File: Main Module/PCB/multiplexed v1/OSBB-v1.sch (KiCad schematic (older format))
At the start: 21 parts, among them P1 AUX 1-3, P14 EXTRA Pins, P2 Wire to Teensy VUSB, P3 +3.3V, P4 Pit limiter, P5 Rotary Encoders, P6 BTN 1-32, Q1 Q_NPN_CBE, Q2 Q_NPN_CBE, Q3 Q_NPN_CBE, U1 74HC4051, U2 74HC4051, U3 74HC4051, U4 74HC4051, U5 Teensy3.2

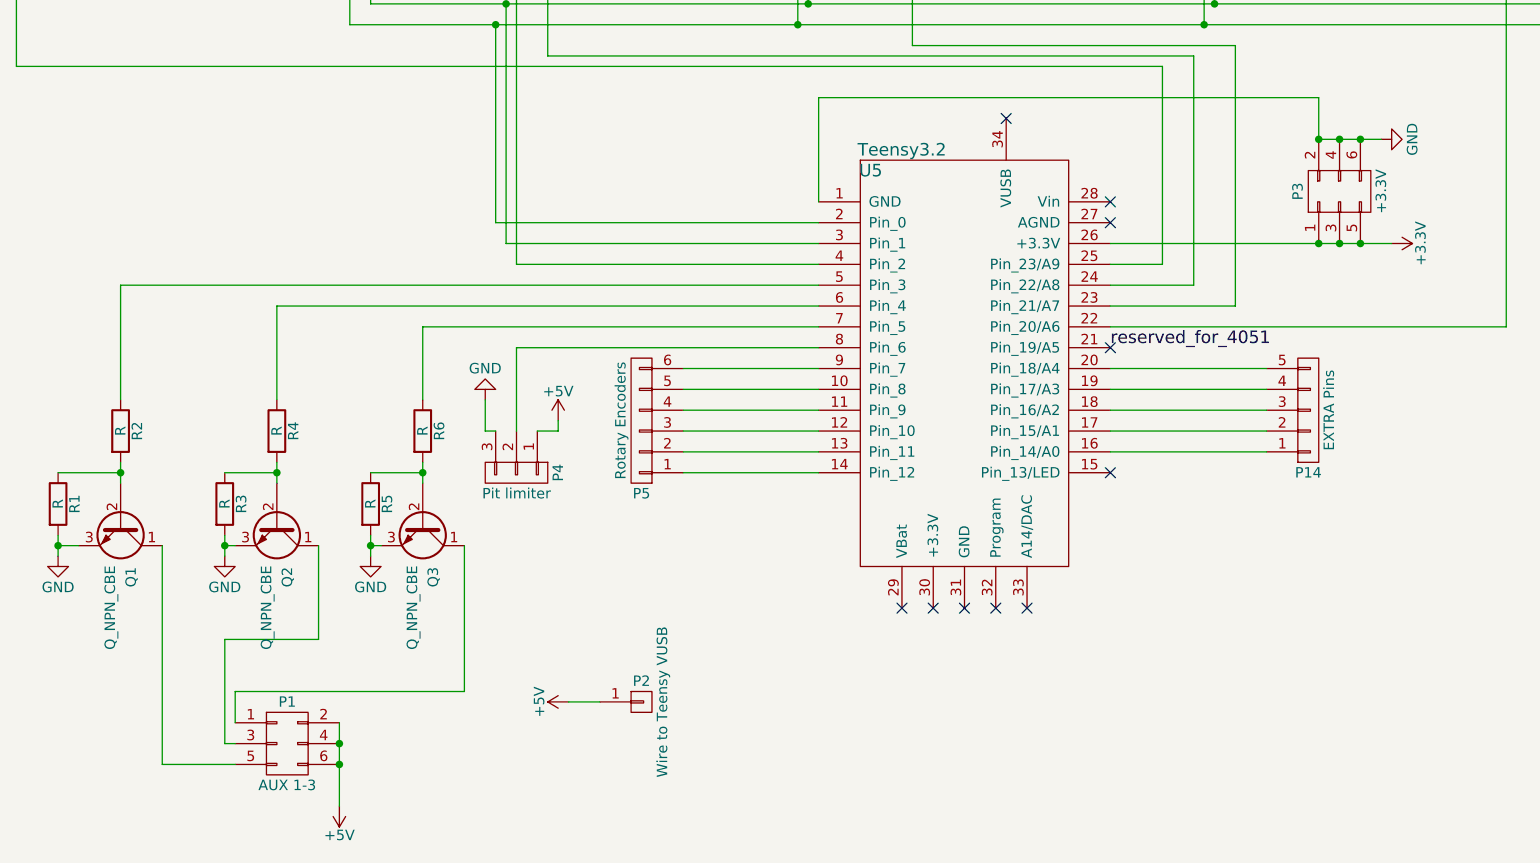
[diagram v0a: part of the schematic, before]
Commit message: * added circuit for pit limiter switch onto the PCB * added open HW logo
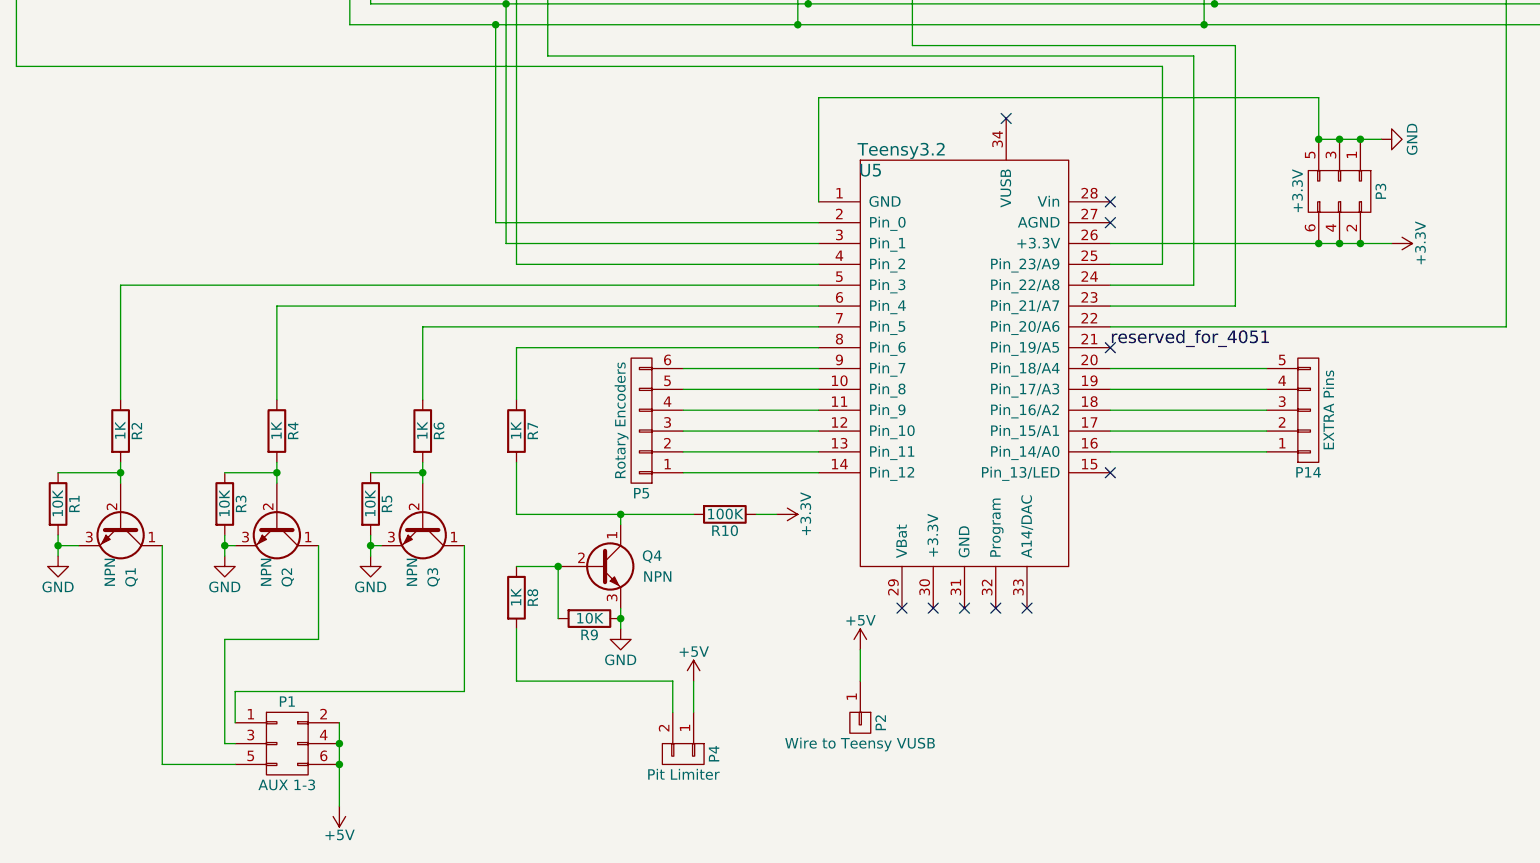
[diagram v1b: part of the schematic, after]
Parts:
- removed P4: Pit limiter, Pin_Headers:Pin_Header_Angled_1x03, symbol CONN_01X03
- added P4: Pit Limiter, Pin_Headers:Pin_Header_Angled_1x02, symbol CONN_01X02
- added Q4: NPN, TO_SOT_Packages_THT:TO-92_Inline_Narrow_Oval, symbol Q_NPN_CBE
- added R10: 100K, Resistors_ThroughHole:Resistor_Horizontal_RM7mm, symbol R
- added R7, R8: 1K, Resistors_ThroughHole:Resistor_Horizontal_RM7mm, symbol R
- added R9: 10K, Resistors_ThroughHole:Resistor_Horizontal_RM7mm, symbol R
- Q1, Q2, Q3: value Q_NPN_CBE -> NPN
- R1, R3, R5: value R -> 10K
- R2, R4, R6: value R -> 1K
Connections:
- net +3V3: now also P3.2 (P2), P3.4 (P4), P3.6 (P6), R10.1; no longer P3.1 (P1), P3.3 (P3), P3.5 (P5)
- net +5V: now also P4.1 (P1)
- net GND: now also P3.1 (P1), P3.3 (P3), P3.5 (P5), Q4.3 (E), R9.1; no longer P3.2 (P2), P3.4 (P4), P3.6 (P6)
- net at U5.8 (Pin_6): now also R7.1
- new net: Q4.1 (C), R10.2, R7.2
- new net: Q4.2 (B), R8.1, R9.2
- new net: P4.2 (P2), R8.2
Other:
- moved on the sheet: P2
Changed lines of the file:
@@
 P 1200 6000
 F 0 "Q1" H 1500 6050 50  0000 R CNN
-F 1 "Q_NPN_CBE" H 1800 5950 50  0000 R CNN
+F 1 "NPN" H 1500 5950 50  0000 R CNN
 F 2 "TO_SOT_Packages_THT:TO-92_Inline_Narrow_Oval" H 1400 6100 50  0001 C CNN
 F 3 "" H 1200 6000 50  0000 C CNN
@@
 P 1950 6000
 F 0 "Q2" H 2250 6050 50  0000 R CNN
-F 1 "Q_NPN_CBE" H 2550 5950 50  0000 R CNN
+F 1 "NPN" H 2250 5950 50  0000 R CNN
 F 2 "TO_SOT_Packages_THT:TO-92_Inline_Narrow_Oval" H 2150 6100 50  0001 C CNN
 F 3 "" H 1950 6000 50  0000 C CNN
@@
 P 2650 6000
 F 0 "Q3" H 2950 6050 50  0000 R CNN
-F 1 "Q_NPN_CBE" H 3250 5950 50  0000 R CNN
+F 1 "NPN" H 2950 5950 50  0000 R CNN
 F 2 "TO_SOT_Packages_THT:TO-92_Inline_Narrow_Oval" H 2850 6100 50  0001 C CNN
 F 3 "" H 2650 6000 50  0000 C CNN
@@
 P 1200 5550
 F 0 "R2" V 1280 5550 50  0000 C CNN
-F 1 "R" V 1200 5550 50  0000 C CNN
+F 1 "1K" V 1200 5550 50  0000 C CNN
 F 2 "Resistors_ThroughHole:Resistor_Horizontal_RM7mm" V 1130 5550 50  0001 C CNN
 F 3 "" H 1200 5550 50  0000 C CNN
@@
 P 1950 5550
 F 0 "R4" V 2030 5550 50  0000 C CNN
-F 1 "R" V 1950 5550 50  0000 C CNN
+F 1 "1K" V 1950 5550 50  0000 C CNN
 F 2 "Resistors_ThroughHole:Resistor_Horizontal_RM7mm" V 1880 5550 50  0001 C CNN
 F 3 "" H 1950 5550 50  0000 C CNN
@@
 P 2650 5550
 F 0 "R6" V 2730 5550 50  0000 C CNN
-F 1 "R" V 2650 5550 50  0000 C CNN
+F 1 "1K" V 2650 5550 50  0000 C CNN
 F 2 "Resistors_ThroughHole:Resistor_Horizontal_RM7mm" V 2580 5550 50  0001 C CNN
 F 3 "" H 2650 5550 50  0000 C CNN
@@
 P 900 5900
 F 0 "R1" V 980 5900 50  0000 C CNN
-F 1 "R" V 900 5900 50  0000 C CNN
+F 1 "10K" V 900 5900 50  0000 C CNN
 F 2 "Resistors_ThroughHole:Resistor_Horizontal_RM7mm" V 830 5900 50  0001 C CNN
 F 3 "" H 900 5900 50  0000 C CNN
@@
 P 1700 5900
 F 0 "R3" V 1780 5900 50  0000 C CNN
-F 1 "R" V 1700 5900 50  0000 C CNN
+F 1 "10K" V 1700 5900 50  0000 C CNN
 F 2 "Resistors_ThroughHole:Resistor_Horizontal_RM7mm" V 1630 5900 50  0001 C CNN
 F 3 "" H 1700 5900 50  0000 C CNN
@@
 P 2400 5900
 F 0 "R5" V 2480 5900 50  0000 C CNN
-F 1 "R" V 2400 5900 50  0000 C CNN
+F 1 "10K" V 2400 5900 50  0000 C CNN
 F 2 "Resistors_ThroughHole:Resistor_Horizontal_RM7mm" V 2330 5900 50  0001 C CNN
 F 3 "" H 2400 5900 50  0000 C CNN
@@
 $EndComp
 $Comp
-L CONN_01X03 P4
-U 1 1 581036AC
-P 3100 5750
-F 0 "P4" H 3100 5950 50  0000 C CNN
-F 1 "Pit limiter" V 3200 5750 50  0000 C CNN
-F 2 "Pin_Headers:Pin_Header_Angled_1x03" H 3100 5750 50  0001 C CNN
-F 3 "" H 3100 5750 50  0000 C CNN
-	1    3100 5750
-	0    1    1    0
-$EndComp
-$Comp
 L GND #PWR04
 U 1 1 5810375B
-P 2950 5400
-F 0 "#PWR04" H 2950 5150 50  0001 C CNN
-F 1 "GND" H 2950 5250 50  0000 C CNN
-F 2 "" H 2950 5400 50  0000 C CNN
-F 3 "" H 2950 5400 50  0000 C CNN
-	1    2950 5400
-	-1   0    0    1
+P 3600 6500
+F 0 "#PWR04" H 3600 6250 50  0001 C CNN
+F 1 "GND" H 3600 6350 50  0000 C CNN
+F 2 "" H 3600 6500 50  0000 C CNN
+F 3 "" H 3600 6500 50  0000 C CNN
+	1    3600 6500
+	1    0    0    -1
 $EndComp
 $Comp
 L +5V #PWR05
 U 1 1 581037AF
-P 3300 5500
-F 0 "#PWR05" H 3300 5350 50  0001 C CNN
-F 1 "+5V" H 3300 5640 50  0000 C CNN
-F 2 "" H 3300 5500 50  0000 C CNN
-F 3 "" H 3300 5500 50  0000 C CNN
-	1    3300 5500
+P 3950 6750
+F 0 "#PWR05" H 3950 6600 50  0001 C CNN
+F 1 "+5V" H 3950 6890 50  0000 C CNN
+F 2 "" H 3950 6750 50  0000 C CNN
+F 3 "" H 3950 6750 50  0000 C CNN
+	1    3950 6750
 	1    0    0    -1
 $EndComp
@@
 	3100 5150 4550 5150
 Wire Wire Line
-	3100 5150 3100 5550
+	3100 5150 3100 5400
 Wire Wire Line
 	6350 3750 6350 4850
 Wire Wire Line
 	700  3800 6200 3800
-Wire Wire Line
-	3000 5550 2950 5550
-Wire Wire Line
-	2950 5550 2950 5400
-Wire Wire Line
-	3200 5550 3300 5550
-Wire Wire Line
-	3300 5550 3300 5500
 Wire Wire Line
 	6200 4750 5950 4750
@@
 L CONN_01X01 P2
 U 1 1 58126797
-P 3700 6850
-F 0 "P2" H 3700 6950 50  0000 C CNN
-F 1 "Wire to Teensy VUSB" V 3800 6850 50  0000 C CNN
-F 2 "Pin_Headers:Pin_Header_Straight_1x01" H 3700 6850 50  0001 C CNN
-F 3 "" H 3700 6850 50  0000 C CNN
-	1    3700 6850
-	1    0    0    -1
+P 4750 6950
+F 0 "P2" H 4750 7050 50  0000 C CNN
+F 1 "Wire to Teensy VUSB" V 4850 6950 50  0000 C CNN
+F 2 "Pin_Headers:Pin_Header_Straight_1x01" H 4750 6950 50  0001 C CNN
+F 3 "" H 4750 6950 50  0000 C CNN
+	1    4750 6950
+	0    1    1    0
 $EndComp
 $Comp
 L +5V #PWR07
 U 1 1 581272E3
-P 3350 6850
-F 0 "#PWR07" H 3350 6700 50  0001 C CNN
-F 1 "+5V" H 3350 6990 50  0000 C CNN
-F 2 "" H 3350 6850 50  0000 C CNN
-F 3 "" H 3350 6850 50  0000 C CNN
-	1    3350 6850
-	0    -1   -1   0
-$EndComp
-Wire Wire Line
-	3500 6850 3350 6850
+P 4750 6600
+F 0 "#PWR07" H 4750 6450 50  0001 C CNN
+F 1 "+5V" H 4750 6740 50  0000 C CNN
+F 2 "" H 4750 6600 50  0000 C CNN
+F 3 "" H 4750 6600 50  0000 C CNN
+	1    4750 6600
+	1    0    0    -1
+$EndComp
 $Comp
 L CONN_02X03 P3
@@
 F 3 "" H 7050 3200 50  0000 C CNN
 	1    7050 4400
-	0    -1   -1   0
+	0    1    1    0
 $EndComp
 Connection ~ 6950 4650
@@
 Wire Wire Line
 	5250 1450 5250 1100
+$Comp
+L Q_NPN_CBE Q4
+U 1 1 5817D9AB
+P 3500 6200
+F 0 "Q4" H 3800 6250 50  0000 R CNN
+F 1 "NPN" H 3850 6150 50  0000 R CNN
+F 2 "TO_SOT_Packages_THT:TO-92_Inline_Narrow_Oval" H 3700 6300 50  0001 C CNN
+F 3 "" H 3500 6200 50  0000 C CNN
+	1    3500 6200
+	1    0    0    -1
+$EndComp
+$Comp
+L R R10
+U 1 1 5817DD3B
+P 4100 5950
+F 0 "R10" V 4180 5950 50  0000 C CNN
+F 1 "100K" V 4100 5950 50  0000 C CNN
+F 2 "Resistors_ThroughHole:Resistor_Horizontal_RM7mm" V 4030 5950 50  0001 C CNN
+F 3 "" H 4100 5950 50  0000 C CNN
+	1    4100 5950
+	0    1    1    0
+$EndComp
+$Comp
+L R R7
+U 1 1 5817DE4E
+P 3100 5550
+F 0 "R7" V 3180 5550 50  0000 C CNN
+F 1 "1K" V 3100 5550 50  0000 C CNN
+F 2 "Resistors_ThroughHole:Resistor_Horizontal_RM7mm" V 3030 5550 50  0001 C CNN
+F 3 "" H 3100 5550 50  0000 C CNN
+	1    3100 5550
+	1    0    0    -1
+$EndComp
+Wire Wire Line
+	3100 5950 3950 5950
+Wire Wire Line
+	3600 5950 3600 6000
+Connection ~ 3600 5950
+Wire Wire Line
+	3100 5950 3100 5700
+Wire Wire Line
+	3100 6750 3850 6750
+$Comp
+L R R8
+U 1 1 58188FA9
+P 3100 6350
+F 0 "R8" V 3180 6350 50  0000 C CNN
+F 1 "1K" V 3100 6350 50  0000 C CNN
+F 2 "Resistors_ThroughHole:Resistor_Horizontal_RM7mm" V 3030 6350 50  0001 C CNN
+F 3 "" H 3100 6350 50  0000 C CNN
+	1    3100 6350
+	1    0    0    -1
+$EndComp
+$Comp
+L CONN_01X02 P4
+U 1 1 58189415
+P 3900 7100
+F 0 "P4" H 3900 7250 50  0000 C CNN
+F 1 "Pit Limiter" V 4000 7100 50  0000 C CNN
+F 2 "Pin_Headers:Pin_Header_Angled_1x02" H 3900 7100 50  0001 C CNN
+F 3 "" H 3900 7100 50  0000 C CNN
+	1    3900 7100
+	0    1    1    0
+$EndComp
+Wire Wire Line
+	3850 6750 3850 6900
+$Comp
+L +3.3V #PWR019
+U 1 1 5818997F
+P 4350 5950
+F 0 "#PWR019" H 4350 5800 50  0001 C CNN
+F 1 "+3.3V" H 4350 6090 50  0000 C CNN
+F 2 "" H 4350 5950 50  0000 C CNN
+F 3 "" H 4350 5950 50  0000 C CNN
+	1    4350 5950
+	0    1    1    0
+$EndComp
+Wire Wire Line
+	4750 6750 4750 6600
+$Comp
+L R R9
+U 1 1 58189FAC
+P 3450 6450
+F 0 "R9" V 3530 6450 50  0000 C CNN
+F 1 "10K" V 3450 6450 50  0000 C CNN
+F 2 "Resistors_ThroughHole:Resistor_Horizontal_RM7mm" V 3380 6450 50  0001 C CNN
+F 3 "" H 3450 6450 50  0000 C CNN
+	1    3450 6450
+	0    1    1    0
+$EndComp
+Wire Wire Line
+	3300 6200 3300 6450
+Wire Wire Line
+	3300 6200 3100 6200
+Wire Wire Line
+	3100 6500 3100 6750
+Connection ~ 3300 6200
+Wire Wire Line
+	3600 6400 3600 6500
+Connection ~ 3600 6450
+Wire Wire Line
+	3950 6750 3950 6900
+Wire Wire Line
+	4250 5950 4350 5950
 $EndSCHEMATC
